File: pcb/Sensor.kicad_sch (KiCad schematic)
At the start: 27 parts, among them IC2 74HC14D-Q100,118, U2 OPA376xxD

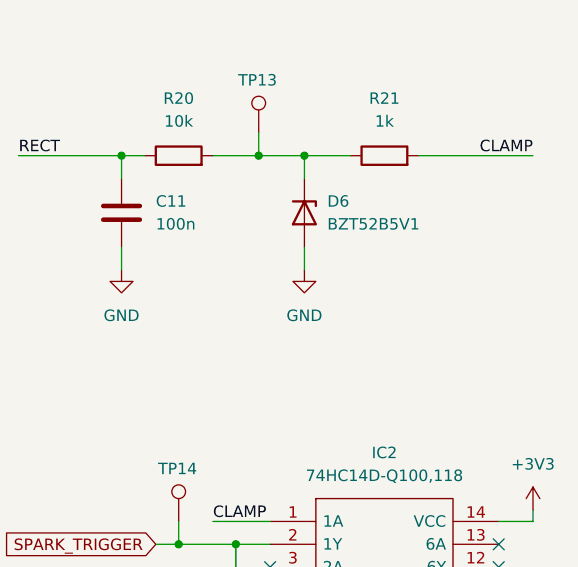
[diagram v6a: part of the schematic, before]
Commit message: added footprints
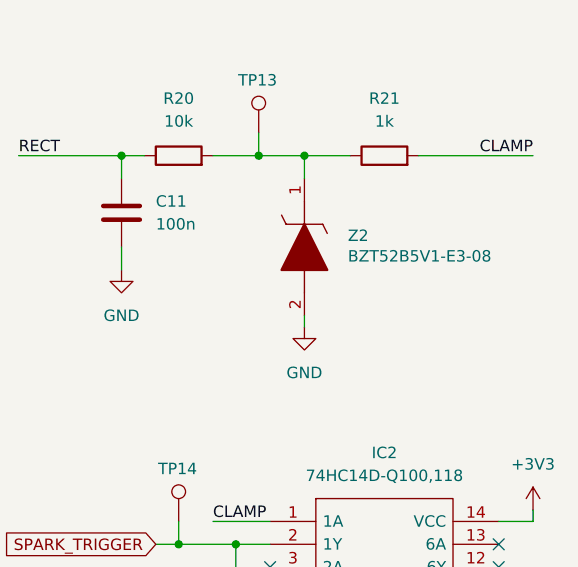
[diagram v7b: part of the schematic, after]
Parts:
- removed D6: BZT52B5V1, symbol Device:D_Zener
- added Z2: BZT52B5V1-E3-08, SamacSys_Parts:BZT52B5V1E308, symbol SamacSys_Parts:BZT52B5V1-E3-08
- BR1: footprint SOP245P670X290-4N -> SamacSys_Parts:SOP245P670X290-4N
- IC2: footprint SOIC127P600X175-14N -> SamacSys_Parts:SOIC127P600X175-14N
- TP12, TP13, TP14: footprint (none) -> Connector_PinHeader_1.00mm:PinHeader_1x01_P1.00mm_Vertical
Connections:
- net GND: now also Z2.2
- net at R20.2, R21.1, TP13.1: now also Z2.1
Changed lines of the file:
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@@
 	(wire
 		(pts
-			(xy 237.49 74.93) (xy 237.49 72.39)
+			(xy 68.58 40.64) (xy 68.58 39.37)
 		)
 		(stroke
@@
 	(wire
 		(pts
-			(xy 68.58 40.64) (xy 68.58 39.37)
+			(xy 217.17 64.77) (xy 217.17 62.23)
 		)
 		(stroke
@@
 	(wire
 		(pts
-			(xy 217.17 64.77) (xy 217.17 62.23)
+			(xy 38.1 96.52) (xy 52.07 96.52)
 		)
 		(stroke
@@
 	(wire
 		(pts
-			(xy 38.1 96.52) (xy 52.07 96.52)
+			(xy 74.93 96.52) (xy 106.68 96.52)
 		)
 		(stroke
@@
 	(wire
 		(pts
-			(xy 74.93 96.52) (xy 106.68 96.52)
+			(xy 223.52 33.02) (xy 217.17 33.02)
 		)
 		(stroke
@@
 	(wire
 		(pts
-			(xy 223.52 33.02) (xy 217.17 33.02)
+			(xy 223.52 105.41) (xy 229.87 105.41)
 		)
 		(stroke
@@
 	(wire
 		(pts
-			(xy 223.52 105.41) (xy 229.87 105.41)
+			(xy 237.49 81.28) (xy 237.49 80.01)
 		)
 		(stroke
@@
 	(symbol
 		(lib_id "power:GND")
-		(at 237.49 74.93 0)
+		(at 237.49 81.28 0)
 		(unit 1)
 		(exclude_from_sim no)
@@
 		(fields_autoplaced yes)
 		(property "Reference" "#PWR017"
-			(at 237.49 81.28 0)
+			(at 237.49 87.63 0)
 			(effects
 				(font
@@
 		)
 		(property "Value" "GND"
-			(at 237.49 80.01 0)
+			(at 237.49 86.36 0)
 			(effects
 				(font
@@
 		)
 		(property "Footprint" ""
-			(at 237.49 74.93 0)
+			(at 237.49 81.28 0)
 			(effects
 				(font
@@
 		)
 		(property "Datasheet" ""
-			(at 237.49 74.93 0)
+			(at 237.49 81.28 0)
 			(effects
 				(font
@@
 		)
 		(property "Description" "Power symbol creates a global label with name \"GND\" , ground"
-			(at 237.49 74.93 0)
+			(at 237.49 81.28 0)
 			(effects
 				(font
@@
 			)
 		)
-		(property "Footprint" "SOIC127P600X175-14N"
+		(property "Footprint" "SamacSys_Parts:SOIC127P600X175-14N"
 			(at 255.27 100.33 0)
 			(effects
@@
 			)
 		)
-		(property "Footprint" ""
+		(property "Footprint" "Connector_PinHeader_1.00mm:PinHeader_1x01_P1.00mm_Vertical"
 			(at 237.49 59.69 0)
 			(effects
@@
 			)
 		)
-		(property "Footprint" ""
+		(property "Footprint" "Connector_PinHeader_1.00mm:PinHeader_1x01_P1.00mm_Vertical"
 			(at 228.6 102.87 0)
 			(effects
@@
 	)
 	(symbol
-		(lib_id "Device:D_Zener")
-		(at 237.49 68.58 270)
-		(unit 1)
-		(exclude_from_sim no)
-		(in_bom yes)
-		(on_board yes)
-		(dnp no)
-		(fields_autoplaced yes)
-		(property "Reference" "D6"
-			(at 240.03 67.3099 90)
-			(effects
-				(font
-					(size 1.27 1.27)
-				)
-				(justify left)
-			)
-		)
-		(property "Value" "BZT52B5V1"
-			(at 240.03 69.8499 90)
-			(effects
-				(font
-					(size 1.27 1.27)
-				)
-				(justify left)
-			)
-		)
-		(property "Footprint" ""
-			(at 237.49 68.58 0)
-			(effects
-				(font
-					(size 1.27 1.27)
-				)
-				(hide yes)
-			)
-		)
-		(property "Datasheet" "~"
-			(at 237.49 68.58 0)
-			(effects
-				(font
-					(size 1.27 1.27)
-				)
-				(hide yes)
-			)
-		)
-		(property "Description" "Zener diode"
-			(at 237.49 68.58 0)
-			(effects
-				(font
-					(size 1.27 1.27)
-				)
-				(hide yes)
-			)
-		)
-		(pin "1"
-		)
-		(pin "2"
-		)
-		(instances
-			(project ""
-				(path "/38d4df77-b5a0-4642-8410-8b13c21c2c3b/4580a192-f0d7-44eb-b345-2965a93c3023"
-					(reference "D6")
-					(unit 1)
-				)
-			)
-		)
-	)
-	(symbol
 		(lib_id "Device:R")
 		(at 34.29 82.55 0)
@@
 			)
 		)
-		(property "Footprint" ""
+		(property "Footprint" "Connector_PinHeader_1.00mm:PinHeader_1x01_P1.00mm_Vertical"
 			(at 222.25 29.21 0)
 			(effects
@@
 	)
 	(symbol
+		(lib_id "SamacSys_Parts:BZT52B5V1-E3-08")
+		(at 237.49 64.77 270)
+		(unit 1)
+		(exclude_from_sim no)
+		(in_bom yes)
+		(on_board yes)
+		(dnp no)
+		(property "Reference" "Z2"
+			(at 242.316 71.12 90)
+			(effects
+				(font
+					(size 1.27 1.27)
+				)
+				(justify left)
+			)
+		)
+		(property "Value" "BZT52B5V1-E3-08"
+			(at 242.316 73.406 90)
+			(effects
+				(font
+					(size 1.27 1.27)
+				)
+				(justify left)
+			)
+		)
+		(property "Footprint" "SamacSys_Parts:BZT52B5V1E308"
+			(at 241.3 74.93 0)
+			(effects
+				(font
+					(size 1.27 1.27)
+				)
+				(justify left)
+				(hide yes)
+			)
+		)
+		(property "Datasheet" "http://www.vishay.com/docs/85760/bzt52.pdf"
+			(at 238.76 74.93 0)
+			(effects
+				(font
+					(size 1.27 1.27)
+				)
+				(justify left)
+				(hide yes)
+			)
+		)
+		(property "Description" "Vishay BZT52B5V1-E3-08 Zener Diode, 5.1V 2% 500 mW SMT 2-Pin SOD-123"
+			(at 237.49 64.77 0)
+			(effects
+				(font
+					(size 1.27 1.27)
+				)
+				(hide yes)
+			)
+		)
+		(property "Description_1" "Vishay BZT52B5V1-E3-08 Zener Diode, 5.1V 2% 500 mW SMT 2-Pin SOD-123"
+			(at 236.22 74.93 0)
+			(effects
+				(font
+					(size 1.27 1.27)
+				)
+				(justify left)
+				(hide yes)
+			)
+		)
+		(property "Height" "1.35"
+			(at 233.68 74.93 0)
+			(effects
+				(font
+					(size 1.27 1.27)
+				)
+				(justify left)
+				(hide yes)
+			)
+		)
+		(property "Manufacturer_Name" "Vishay"
+			(at 231.14 74.93 0)
+			(effects
+				(font
+					(size 1.27 1.27)
+				)
+				(justify left)
+				(hide yes)
+			)
+		)
+		(property "Manufacturer_Part_Number" "BZT52B5V1-E3-08"
+			(at 228.6 74.93 0)
+			(effects
+				(font
+					(size 1.27 1.27)
+				)
+				(justify left)
+				(hide yes)
+			)
+		)
+		(property "Mouser Part Number" "78-BZT52B5V1-E3-08"
+			(at 226.06 74.93 0)
+			(effects
+				(font
+					(size 1.27 1.27)
+				)
+				(justify left)
+				(hide yes)
+			)
+		)
+		(property "Mouser Price/Stock" "https://www.mouser.co.uk/ProductDetail/Vishay-Semiconductors/BZT52B5V1-E3-08?qs=KP8Io%2FXyE5Sz55z44LM67w%3D%3D"
+			(at 223.52 74.93 0)
+			(effects
+				(font
+					(size 1.27 1.27)
+				)
+				(justify left)
+				(hide yes)
+			)
+		)
+		(property "Arrow Part Number" "BZT52B5V1-E3-08"
+			(at 220.98 74.93 0)
+			(effects
+				(font
+					(size 1.27 1.27)
+				)
+				(justify left)
+				(hide yes)
+			)
+		)
+		(property "Arrow Price/Stock" "https://www.arrow.com/en/products/bzt52b5v1-e3-08/vishay?utm_currency=USD&region=nac"
+			(at 218.44 74.93 0)
+			(effects
+				(font
+					(size 1.27 1.27)
+				)
+				(justify left)
+				(hide yes)
+			)
+		)
+		(pin "2"
+		)
+		(pin "1"
+		)
+		(instances
+			(project "ecu-dev-board"
+				(path "/38d4df77-b5a0-4642-8410-8b13c21c2c3b/4580a192-f0d7-44eb-b345-2965a93c3023"
+					(reference "Z2")
+					(unit 1)
+				)
+			)
+		)
+	)
+	(symbol
 		(lib_id "Jumper:SolderJumper_2_Open")
 		(at 73.66 152.4 180)
@@
 			)
 		)
-		(property "Footprint" "SOP245P670X290-4N"
+		(property "Footprint" "SamacSys_Parts:SOP245P670X290-4N"
 			(at 238.76 38.1 0)
 			(effects

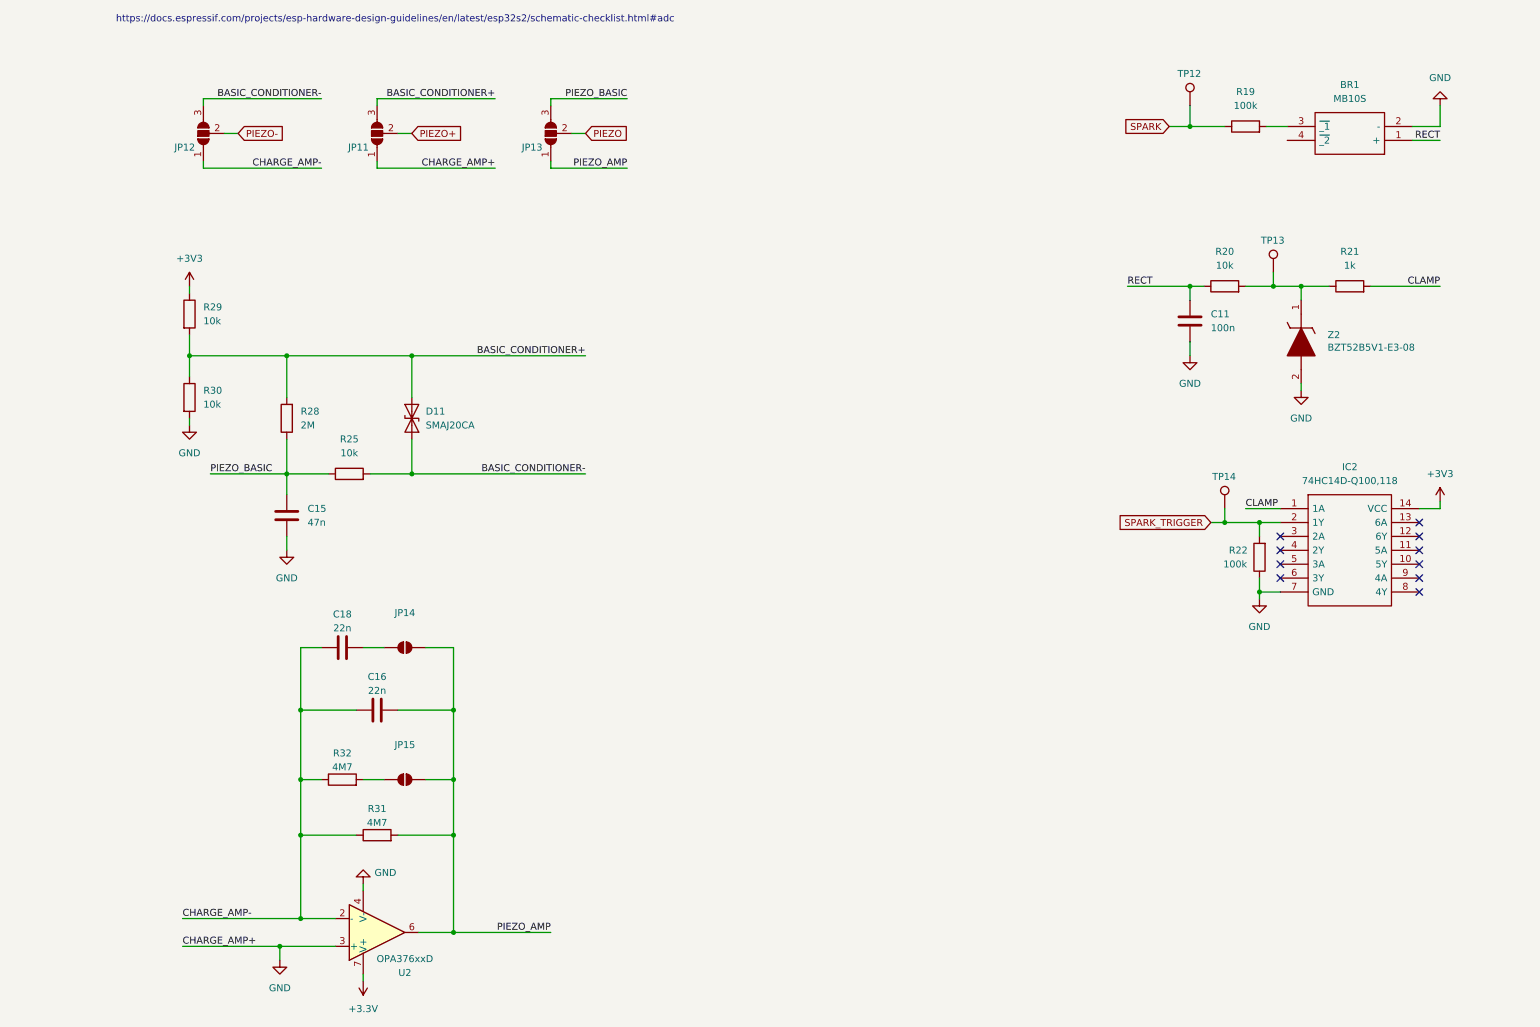
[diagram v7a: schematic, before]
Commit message: added SCR from kill switch to GND and RGB led
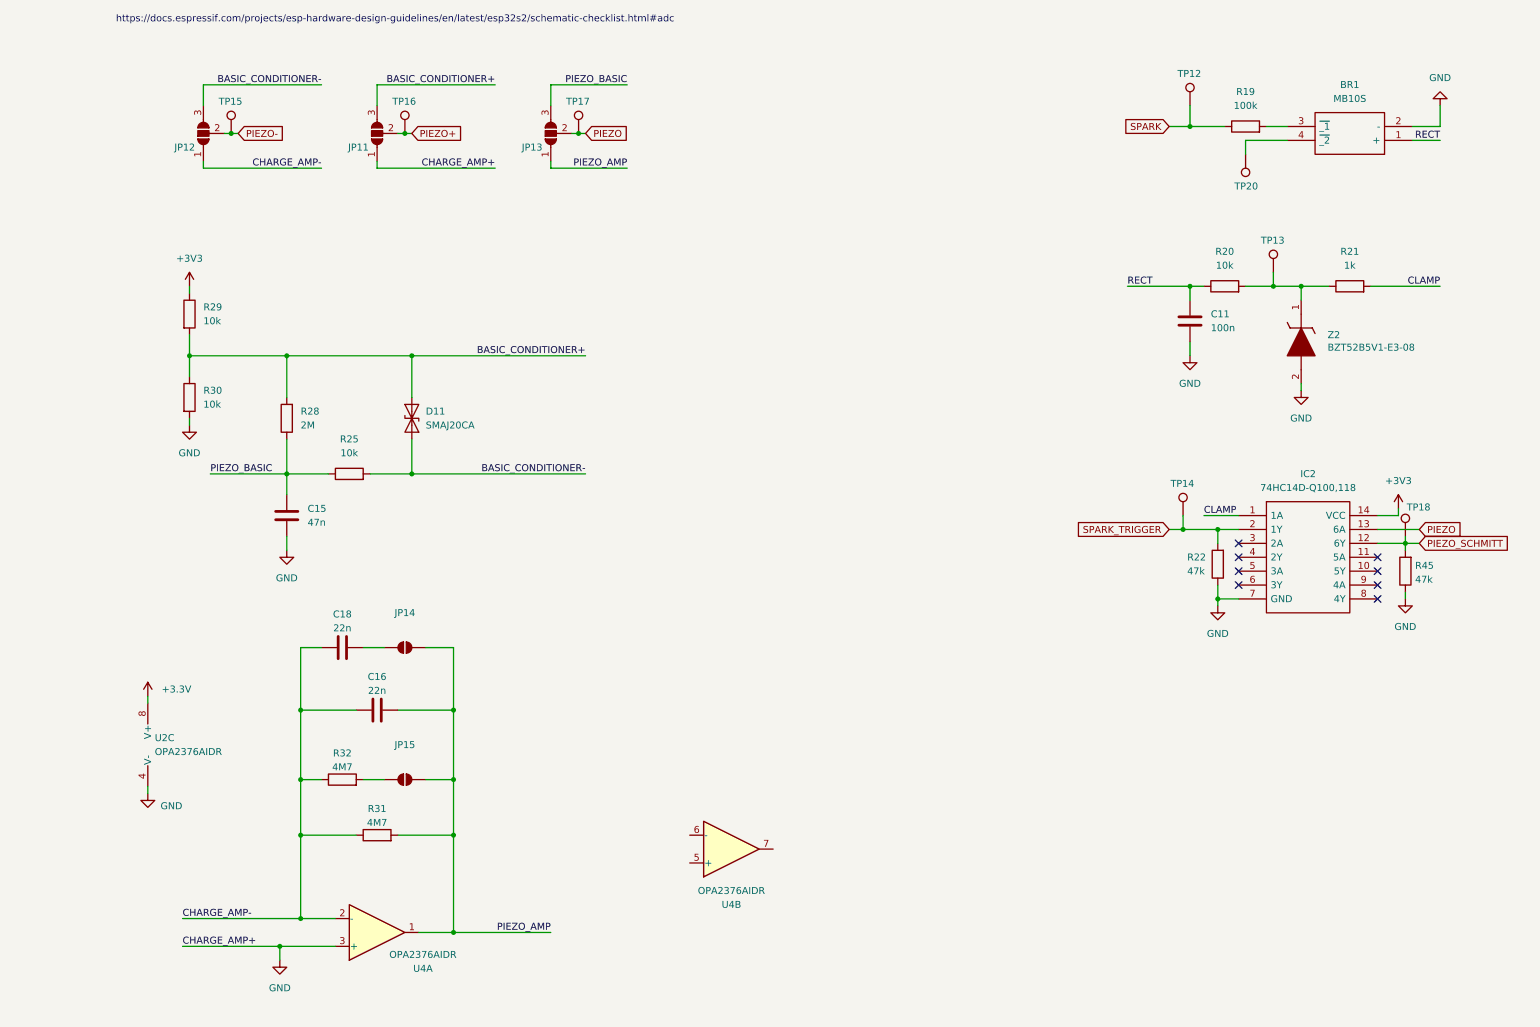
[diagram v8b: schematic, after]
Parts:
- removed U2: OPA376xxD, Package_SO:SOIC-8_3.9x4.9mm_P1.27mm, symbol Amplifier_Operational:OPA376xxD
- added R45: 47k, Resistor_SMD:R_0201_0603Metric, symbol Device:R
- added TP15, TP16, TP17, TP18, TP20: TestPoint, Connector_PinHeader_1.00mm:PinHeader_1x01_P1.00mm_Vertical, symbol Connector:TestPoint
- added U2, U4: OPA2376AIDR, symbol Amplifier_Operational:OPA2376xxD
- R22: value 100k -> 47k
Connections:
- net +3.3V: now also U2.8 (V+)
- net CHARGE_AMP-: now also U4.2 (-)
- net GND: now also R45.1, U2.4 (V-), U4.3 (+)
- net PIEZO: now also IC2.13 (6A), TP17.1
- net PIEZO+: now also TP16.1
- net PIEZO-: now also TP15.1
- net PIEZO_AMP: now also U4.1
- net PIEZO_SCHMITT: now reaches IC2.12 (6Y)
- net PIEZO_SCHMITT: now also R45.2, TP18.1
- net at BR1.4 (~{_2}): now also TP20.1
- no-connect marks 10 -> 8
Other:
- moved on the sheet: IC2, R22, TP14
